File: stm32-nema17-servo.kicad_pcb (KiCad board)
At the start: 2 copper layers, 42 x 42 mm, 91 parts, among them J1 Conn_01x05, J2 C31-S-RA-CS1A-BK-SS, J3 TC-2050, J4 Screw_Terminal_01x02, J5 Screw_Terminal_01x02, J7 Conn_01x03, J8 Conn_01x03, J9 Conn_01x02, M1 Stepper_Motor_bipolar, Q1 NTTFS4937N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

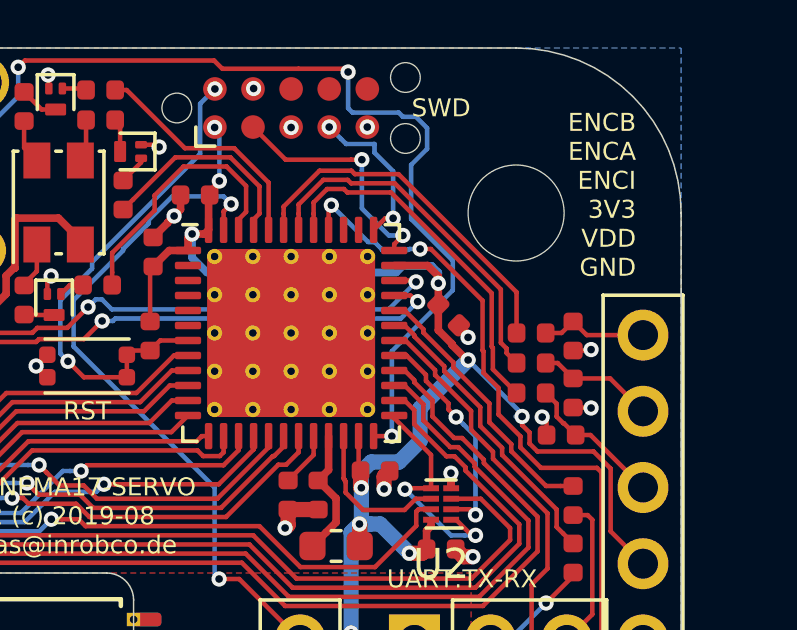
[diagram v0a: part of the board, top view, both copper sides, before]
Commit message: board layout improvements and firmware that finally shows up as USB CDC device
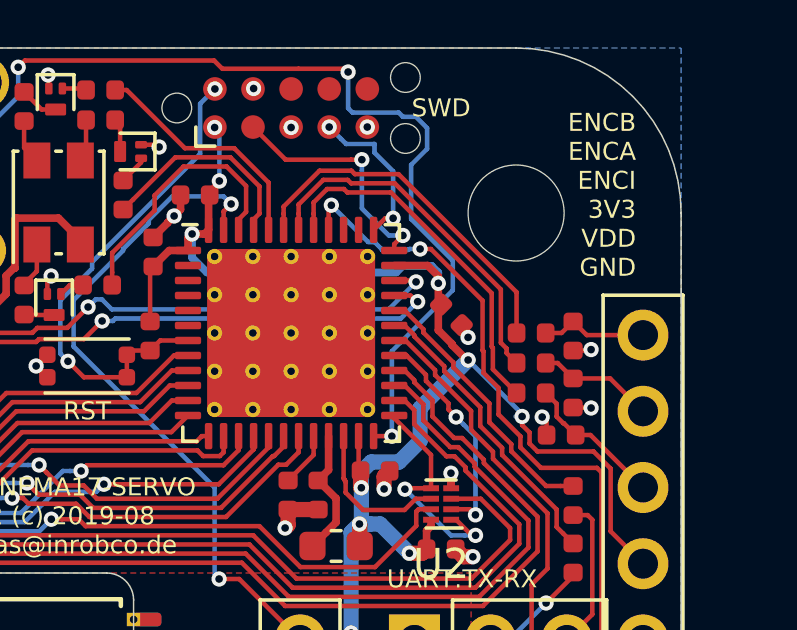
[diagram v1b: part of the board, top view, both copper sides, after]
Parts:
- moved C3 0.09 mm to (163.3, 107.9)
